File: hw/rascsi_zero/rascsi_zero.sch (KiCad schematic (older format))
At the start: 88 parts, among them IC1 SN74LS641-1DW, IC2 SN74LS641-1DW, IC3 SN74LS641-1DW, IC4 SN74LS641-1DW, J1 Raspberry_Pi_2_3, J2 DNP, J4 I2C Pinout, J6 CONNFLY DB-25, J7 DNP, X1 Mac, X2 Dogcow, X3 Mac, X4 Dogcow, X5 Dogcow, X6 Dogcow, X7 Pi, X8 Pi

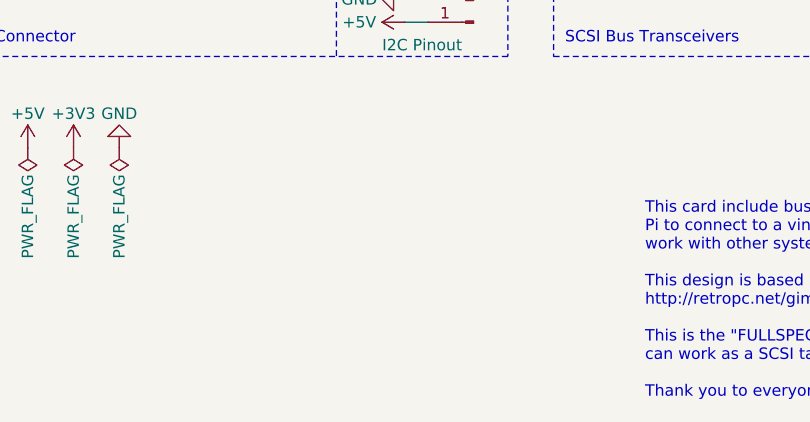
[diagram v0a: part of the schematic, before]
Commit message: Add USB C Port
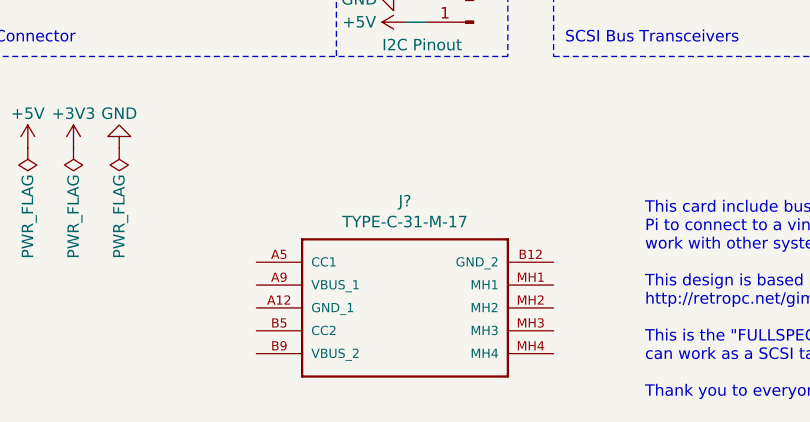
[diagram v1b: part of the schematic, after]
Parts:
- added J?: TYPE-C-31-M-17, TYPEC31M17, symbol TYPE-C-31-M-17:TYPE-C-31-M-17
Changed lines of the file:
@@
 	0    -1   -1   0
 $EndComp
+$Comp
+L TYPE-C-31-M-17:TYPE-C-31-M-17 J?
+U 1 1 618FD321
+P 2200 7300
+F 0 "J?" H 2850 7567 50  0000 C CNN
+F 1 "TYPE-C-31-M-17" H 2850 7476 50  0000 C CNN
+F 2 "TYPEC31M17" H 2200 7300 50  0001 L BNN
+F 3 "" H 2200 7300 50  0001 L BNN
+F 4 "3.26mm" H 2200 7300 50  0001 L BNN "HEIGHT"
+F 5 "" H 2200 7300 50  0001 L BNN "MOUSER_PART_NUMBER"
+F 6 "" H 2200 7300 50  0001 L BNN "RS_PRICE-STOCK"
+F 7 "USB Connectors 6 Receptacle 1 RoHS" H 2200 7300 50  0001 L BNN "DESCRIPTION"
+F 8 "Korean Hroparts Elec" H 2200 7300 50  0001 L BNN "MANUFACTURER_NAME"
+F 9 "TYPE-C-31-M-17" H 2200 7300 50  0001 L BNN "MANUFACTURER_PART_NUMBER"
+F 10 "" H 2200 7300 50  0001 L BNN "RS_PART_NUMBER"
+F 11 "" H 2200 7300 50  0001 L BNN "MOUSER_PRICE-STOCK"
+F 12 "C283540" H 2200 7300 50  0001 C CNN "LCSC"
+	1    2200 7300
+	1    0    0    -1
+$EndComp
 $EndSCHEMATC

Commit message: Routed and cleaned up USB C port
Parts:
- removed X1, X3: Mac, SamacSys_Parts:mac_happy_small, symbol SamacSys_Parts:Logo
- removed X8: Pi, SamacSys_Parts:scsi_logo, symbol SamacSys_Parts:Logo
- H1, H2, H3, H4: footprint MountingHole:MountingHole_2.7mm_M2.5_Pad_Via -> MountingHole:MountingHole_2.7mm_M2.5_Pad; symbol Mechanical:MountingHole_Pad -> Mechanical:MountingHole
- gave numbers to parts that had none: 1
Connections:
- net +5V: now also J3.A9 (VBUS_1), J3.B9 (VBUS_2)
- net GND: now also J3.A12 (GND_1), J3.B12 (GND_2), J3.MH1, J3.MH2, J3.MH3, J3.MH4; no longer H1.1, H2.1, H3.1, H4.1
- no-connect marks 3 -> 5
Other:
- note added: "1.0"
- note added: "10-Nov-2021"
- note added: "5v Power Connector"
- note added: "RaSCSI Reloaded - Zero"
- note removed: "2.4"
- note removed: "28-Dec-2020"
- note removed: "Aux 5v Power Connector"
- note removed: "RaSCSI - 68kmla Edition"
- moved on the sheet: D5, FUSE1, J3

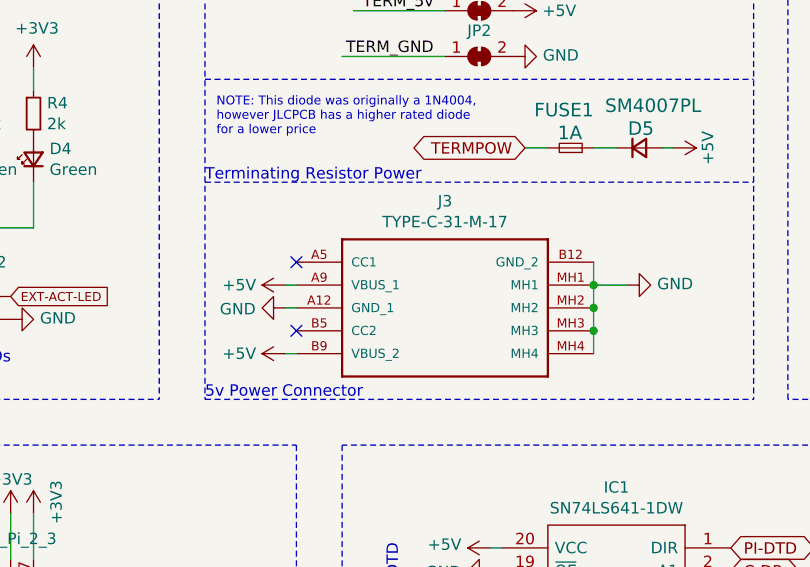
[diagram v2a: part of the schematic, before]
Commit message: Changed USB port back to Micro. As-ordered 1p0
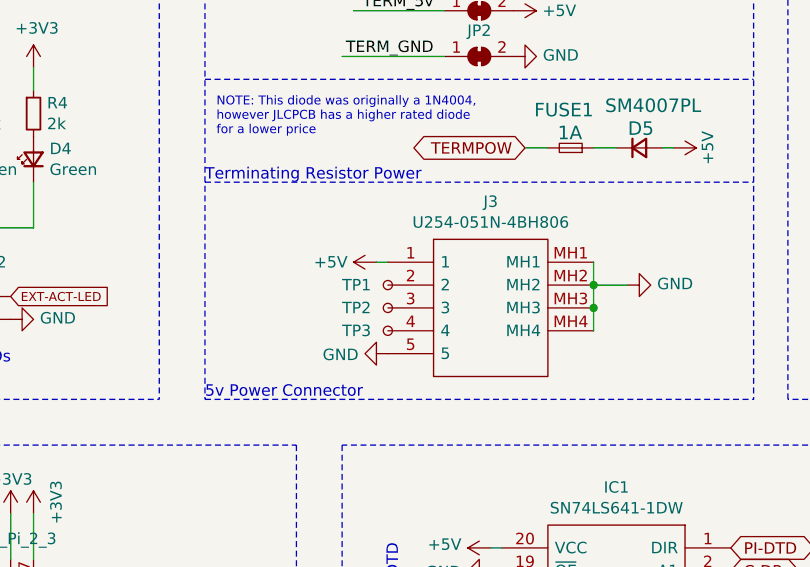
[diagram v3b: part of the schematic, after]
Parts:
- removed J3: TYPE-C-31-M-17, TYPEC31M17, symbol TYPE-C-31-M-17:TYPE-C-31-M-17
- added J3: U254-051N-4BH806, U254051N4BH806, symbol SamacSys_Parts:U254-051N-4BH806
- added TP1, TP2, TP3: TestPoint_Small, TestPoint:TestPoint_Pad_D1.0mm, symbol Connector:TestPoint_Small
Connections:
- net +5V: now also J3.1
- net GND: now also J3.5, J3.MH1, J3.MH2, J3.MH3, J3.MH4
- new net: J3.2, TP1.1
- new net: J3.3, TP2.1
- new net: J3.4, TP3.1
- no-connect marks 5 -> 3
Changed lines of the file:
@@
 	0    -1   -1   0
-$EndComp
-$Comp
-L TYPE-C-31-M-17:TYPE-C-31-M-17 J3
-U 1 1 618FD321
-P 3300 1850
-F 0 "J3" H 3950 2117 50  0000 C CNN
-F 1 "TYPE-C-31-M-17" H 3950 2026 50  0000 C CNN
-F 2 "TYPEC31M17" H 3300 1850 50  0001 L BNN
-F 3 "" H 3300 1850 50  0001 L BNN
-F 4 "3.26mm" H 3300 1850 50  0001 L BNN "HEIGHT"
-F 5 "" H 3300 1850 50  0001 L BNN "MOUSER_PART_NUMBER"
-F 6 "" H 3300 1850 50  0001 L BNN "RS_PRICE-STOCK"
-F 7 "USB Connectors 6 Receptacle 1 RoHS" H 3300 1850 50  0001 L BNN "DESCRIPTION"
-F 8 "Korean Hroparts Elec" H 3300 1850 50  0001 L BNN "MANUFACTURER_NAME"
-F 9 "TYPE-C-31-M-17" H 3300 1850 50  0001 L BNN "MANUFACTURER_PART_NUMBER"
-F 10 "" H 3300 1850 50  0001 L BNN "RS_PART_NUMBER"
-F 11 "" H 3300 1850 50  0001 L BNN "MOUSER_PRICE-STOCK"
-F 12 "C283540" H 3300 1850 50  0001 C CNN "LCSC"
-	1    3300 1850
-	1    0    0    -1
 $EndComp
 Text Notes 2950 1300 0    39   ~ 0
@@
 L power:+5V #PWR013
 U 1 1 6195FDC1
-P 3250 1950
-F 0 "#PWR013" H 3250 1800 50  0001 C CNN
-F 1 "+5V" V 3250 2150 50  0000 C CNN
-F 2 "" H 3250 1950 50  0001 C CNN
-F 3 "" H 3250 1950 50  0001 C CNN
-	1    3250 1950
+P 3650 1850
+F 0 "#PWR013" H 3650 1700 50  0001 C CNN
+F 1 "+5V" V 3650 2050 50  0000 C CNN
+F 2 "" H 3650 1850 50  0001 C CNN
+F 3 "" H 3650 1850 50  0001 C CNN
+	1    3650 1850
 	0    -1   -1   0
 $EndComp
@@
 $EndComp
 $Comp
-L power:+5V #PWR015
-U 1 1 61982243
-P 3250 2250
-F 0 "#PWR015" H 3250 2100 50  0001 C CNN
-F 1 "+5V" V 3250 2450 50  0000 C CNN
-F 2 "" H 3250 2250 50  0001 C CNN
-F 3 "" H 3250 2250 50  0001 C CNN
-	1    3250 2250
-	0    -1   -1   0
-$EndComp
-NoConn ~ 3300 2150
-NoConn ~ 3300 1850
-$Comp
 L power:GND #PWR014
 U 1 1 619E6836
-P 3250 2050
-F 0 "#PWR014" H 3250 1800 50  0001 C CNN
-F 1 "GND" V 3255 1922 50  0000 R CNN
-F 2 "" H 3250 2050 50  0001 C CNN
-F 3 "" H 3250 2050 50  0001 C CNN
-	1    3250 2050
+P 3700 2250
+F 0 "#PWR014" H 3700 2000 50  0001 C CNN
+F 1 "GND" V 3705 2122 50  0000 R CNN
+F 2 "" H 3700 2250 50  0001 C CNN
+F 3 "" H 3700 2250 50  0001 C CNN
+	1    3700 2250
 	0    1    1    0
 $EndComp
@@
 Connection ~ 4600 1950
 Wire Wire Line
-	4600 1950 4600 2050
-Connection ~ 4600 2050
-Wire Wire Line
-	4600 2050 4600 2150
-Connection ~ 4600 2150
-Wire Wire Line
-	4600 2150 4600 2250
-Wire Wire Line
 	4750 1950 4600 1950
 Wire Wire Line
-	3250 1950 3300 1950
-Wire Wire Line
-	3300 2050 3250 2050
-Wire Wire Line
-	3250 2250 3300 2250
+	3650 1850 3700 1850
 Wire Wire Line
 	7850 7700 7850 7750
 Wire Wire Line
 	7550 7700 7850 7700
+$Comp
+L Connector:TestPoint_Small TP1
+U 1 1 619F9EC9
+P 3700 1950
+F 0 "TP1" H 3500 1950 50  0000 L CNN
+F 1 "TestPoint_Small" H 3652 1995 50  0001 R CNN
+F 2 "TestPoint:TestPoint_Pad_D1.0mm" H 3900 1950 50  0001 C CNN
+F 3 "~" H 3900 1950 50  0001 C CNN
+	1    3700 1950
+	1    0    0    -1
+$EndComp
+Wire Wire Line
+	4600 2050 4600 2150
+Wire Wire Line
+	4600 1950 4600 2050
+Connection ~ 4600 2050
+$Comp
+L SamacSys_Parts:U254-051N-4BH806 J3
+U 1 1 61943FE1
+P 3700 1850
+F 0 "J3" H 4150 2115 50  0000 C CNN
+F 1 "U254-051N-4BH806" H 4150 2024 50  0000 C CNN
+F 2 "U254051N4BH806" H 4450 1950 50  0001 L CNN
+F 3 "https://datasheet.lcsc.com/szlcsc/XKB-U254-051N-4BH806_C319170.pdf" H 4450 1850 50  0001 L CNN
+F 4 "USB Connectors SMD RoHS" H 4450 1750 50  0001 L CNN "Description"
+F 5 "3" H 4450 1650 50  0001 L CNN "Height"
+F 6 "XKB Enterprise" H 4450 1550 50  0001 L CNN "Manufacturer_Name"
+F 7 "U254-051N-4BH806" H 4450 1450 50  0001 L CNN "Manufacturer_Part_Number"
+F 8 "U254-051N-4BH806" H 4450 1350 50  0001 L CNN "Arrow Part Number"
+F 9 "" H 4450 1250 50  0001 L CNN "Arrow Price/Stock"
+F 10 "" H 4450 1150 50  0001 L CNN "Mouser Part Number"
+F 11 "" H 4450 1050 50  0001 L CNN "Mouser Price/Stock"
+F 12 "C319170" H 3700 1850 50  0001 C CNN "LCSC"
+	1    3700 1850
+	1    0    0    -1
+$EndComp
+$Comp
+L Connector:TestPoint_Small TP2
+U 1 1 61A21563
+P 3700 2050
+F 0 "TP2" H 3500 2050 50  0000 L CNN
+F 1 "TestPoint_Small" H 3652 2095 50  0001 R CNN
+F 2 "TestPoint:TestPoint_Pad_D1.0mm" H 3900 2050 50  0001 C CNN
+F 3 "~" H 3900 2050 50  0001 C CNN
+	1    3700 2050
+	1    0    0    -1
+$EndComp
+$Comp
+L Connector:TestPoint_Small TP3
+U 1 1 61A2241A
+P 3700 2150
+F 0 "TP3" H 3500 2150 50  0000 L CNN
+F 1 "TestPoint_Small" H 3652 2195 50  0001 R CNN
+F 2 "TestPoint:TestPoint_Pad_D1.0mm" H 3900 2150 50  0001 C CNN
+F 3 "~" H 3900 2150 50  0001 C CNN
+	1    3700 2150
+	1    0    0    -1
+$EndComp
 $EndSCHEMATC
